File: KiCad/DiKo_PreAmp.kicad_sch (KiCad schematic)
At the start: 17 parts, among them J1 VCC_IN, J2 VCC_OUT, SW1 SW_DPST, U1 REC10K

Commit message: KiCad
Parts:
- added C11: 100nF, symbol Device:C_Small
- added C12, C13: 470pF, symbol Device:C_Small
- added C14, C15: 1nF, symbol Device:C_Small
- added L3: L_Ferrite, symbol Device:L_Ferrite
- added L5: ~, symbol Device:L_Ferrite
- added U2: REC10K-2409, REC10K-2409SAW_H2:CONV_REC10K-2409SAW_H2, symbol REC10K-2409SAW_H2:REC10K-2409SAW_H2
- U1: value REC10K -> REC10K-2415
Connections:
- net FILT_GND: now also C14.1, C15.2
- net GND: now also C11.2, C13.2, C15.1, L5.2
- net at C2.1, C8.2, C9.1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: now also C12.1, U2.1 (+VIN)
- net at C10.1, C2.2, C7.1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: now also C13.1, U2.2 (-VIN)
- new net: L5.1, U2.4 (-VOUT)
- new net: L3.1, U2.6 (+VOUT)
- new net +9V: C11.1, C12.2, C14.2, L3.2
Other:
- moved on the sheet: C10, C3, C4, C5, C6, C9, L1, L2, U1

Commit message: Einpflegen der Eingangsstufe
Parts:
- added C16: 47u, symbol Device:C_Small
- added C17, C18: 0.1uF, symbol Device:C_Small
- added J3: Mic_In, symbol Connector:Conn_01x03_Pin
- added R1, R2: 47k, symbol Device:R_US
- added R3: 100k, symbol Device:R_US
- added R4: 22R, symbol Device:R_US
- added RV1: 10k lin, symbol Device:R_Potentiometer_US
- added U3: INA128U, D0008A_N, symbol INA128U:INA128U
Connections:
- net +15V: now also C18.2, U3.7 (V+)
- net -15V: now also C17.2, U3.4 (V-)
- net GND: now also C17.1, C18.1, J3.1 (Pin_1), R1.2, R2.2, R3.2, U3.5 (REF)
- new net: J3.3 (Pin_3), R1.1, U3.2 (IN-)
- new net: J3.2 (Pin_2), R2.1, U3.3 (IN+)
- new net: C16.1, R3.1
- new net: RV1.1, U3.1 (RG)
- new net: RV1.2, RV1.3, U3.8 (RG)
- new net: C16.2, R4.2
- new net: R4.1, U3.6 (OUT)
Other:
- moved on the sheet: C1, C10, C11, C12, C13, C14, C15, C2, C3, C4, C5, C6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

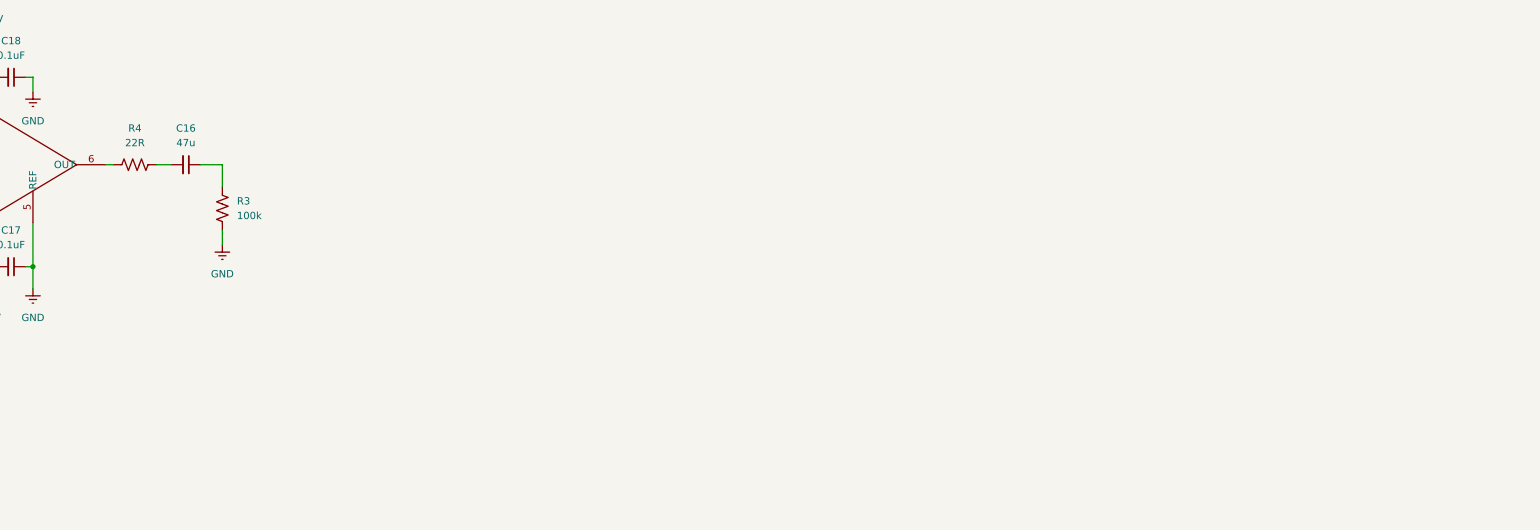
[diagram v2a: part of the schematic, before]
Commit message: Eingangsstufe update
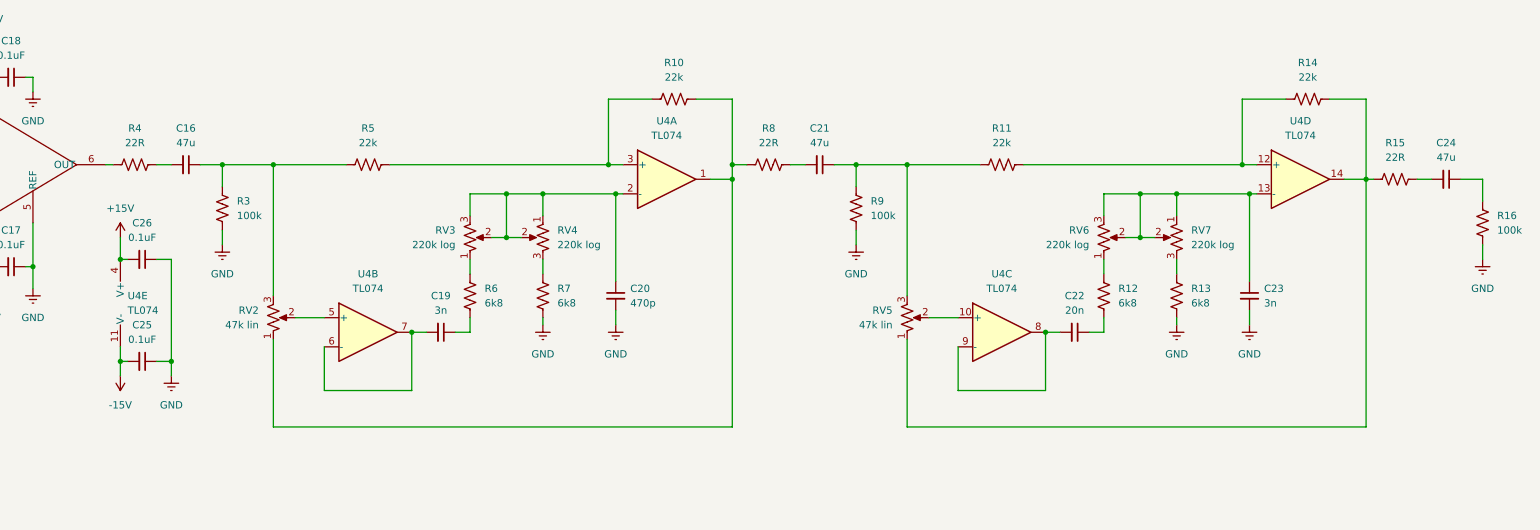
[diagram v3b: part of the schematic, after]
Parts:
- added C19, C23: 3n, symbol Device:C_Small
- added C20: 470p, symbol Device:C_Small
- added C21, C24: 47u, symbol Device:C_Small
- added C22: 20n, symbol Device:C_Small
- added C25, C26: 0.1uF, symbol Device:C_Small
- added R10, R11, R14, R5: 22k, symbol Device:R_US
- added R12, R13, R6, R7: 6k8, symbol Device:R_US
- added R15, R8: 22R, symbol Device:R_US
- added R16, R9: 100k, symbol Device:R_US
- added RV2, RV5: 47k lin, symbol Device:R_Potentiometer_US
- added RV3, RV4, RV6, RV7: 220k log, symbol Device:R_Potentiometer_US
- added U4: TL074, symbol Amplifier_Operational:TL074
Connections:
- net +15V: now also C26.2, U4.4 (V+)
- net -15V: now also C25.2, U4.11 (V-)
- net GND: now also C20.2, C23.2, C25.1, C26.1, R13.2, R16.2, R7.2, R9.2
- net at C16.1, R3.1: now also R5.1, RV2.3
- new net: RV5.2, U4.10 (+)
- new net: C22.2, U4.8, U4.9 (-)
- new net: R6.1, RV3.1
- new net: C20.1, RV3.2, RV3.3, RV4.1, RV4.2, U4.2 (-)
- new net: R10.2, R8.1, RV2.1, U4.1
- new net: RV2.2, U4.5 (+)
- new net: R10.1, R5.2, U4.3 (+)
- new net: C19.2, U4.6 (-), U4.7
- new net: R13.1, RV7.3
- new net: R11.2, R14.1, U4.12 (+)
- new net: C23.1, RV6.2, RV6.3, RV7.1, RV7.2, U4.13 (-)
- new net: R14.2, R15.1, RV5.1, U4.14
- new net: R12.1, RV6.1
- new net: C19.1, R6.2
- new net: C21.1, R11.1, R9.1, RV5.3
- new net: R7.1, RV4.3
- new net: C21.2, R8.2
- new net: C22.1, R12.2
- new net: C24.1, R16.1
- new net: C24.2, R15.2

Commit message: Eingangsstufe Update
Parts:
- added C27, C28, C29, C30, C31, C36, C37, C38, C41, C48, C50, C51, C52, C55, C56, C57: 47u, symbol Device:C_Small
- added C32, C33, C39, C40, C45, C46, C53, C54: 0.1uF, symbol Device:C_Small
- added C34, C35: 330p, symbol Device:C_Small
- added C42: 33u, symbol Device:C_Small
- added C43: 150n, symbol Device:C_Small
- added C44: 470n, symbol Device:C_Small
- added C47, C49: 15p, symbol Device:C_Small
- added J4: R_Line_In, symbol Connector:Conn_01x02_Pin
- added J5: L_Line_In, symbol Connector:Conn_01x02_Pin
- added J6: R_Phono_In, symbol Connector:Conn_01x02_Pin
- added J7: L_Phono_In, symbol Connector:Conn_01x02_Pin
- added J8: Effekt_In, symbol Connector:Conn_01x02_Pin
- added R17: 100R, symbol Device:R_US
- added R18, R21, R22, R24, R27, R33, R34, R38, R42, R47, R49, R51, R54, R61, R64, R71: 100k, symbol Device:R_US
- added R19, R20, R23, R25, R26, R28, R39, R43, R48, R50, R62, R65, R72: 22R, symbol Device:R_US
- added R29, R31: 47k, symbol Device:R_US
- added R30, R32: 0R, symbol Device:R_US
- added R35, R36, R37, R52, R53, R55, R56, R59, R60, R63, R66, R67, R70: 10k, symbol Device:R_US
- added R40, R45: 22k, symbol Device:R_US
- added R41: 1k, symbol Device:R_US
- added R44: 690R, symbol Device:R_US
- added R46: 1k2, symbol Device:R_US
- added R57, R58, R68, R69: 5k, symbol Device:R_US
- added SW2, SW3, SW4: SW_SPDT, symbol Switch:SW_SPDT
- added U5, U6, U7, U8: TL074, symbol Amplifier_Operational:TL074
- R15: value 22R -> 10k
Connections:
- net +15V: now also C32.2, C39.2, C45.2, C53.2, U5.4 (V+), U6.4 (V+), U7.4 (V+), U8.4 (V+)
- net -15V: now also C33.2, C40.2, C46.2, C54.2, U5.11 (V-), U6.11 (V-), U7.11 (V-), U8.11 (V-)
- net GND: now also C32.1, C33.1, C34.2, C35.2, C39.1, C40.1, C42.2, C43.2, C45.1, C46.1, C53.1, C54.1, J4.2 (Pin_2), J5.2 (Pin_2), J6.2 (Pin_2), J7.2 (Pin_2), J8.2 (Pin_2), R18.2, R21.2, R22.2, R24.2, R27.2, R29.2, R31.2, R33.2, R34.2, R38.2, R42.2, R44.2, R46.2, R47.2, R49.2, R51.2, R54.2, R58.1, R61.2, R64.2, R69.1, R71.2, U5.10 (+), U6.10 (+), U7.10 (+), U8.12 (+)
- net at R10.2, RV2.1, U4.1: now also C21.2; no longer R8.1
- net at R5.1, RV2.3: now also R4.2; no longer C16.1, R3.1
- net at R14.2, RV5.1, U4.14: now also C24.2; no longer R15.1
- net at RV1.2, RV1.3: now also R17.1; no longer U3.8 (RG)
- net at R11.1, RV5.3: now also R8.2; no longer C21.1, R9.1
- net at C24.1, R16.1: now also R15.1
- net at R15.2: now also R52.2, R53.1, U7.9 (-); no longer C24.2
- net at C16.2: now also U3.6 (OUT); no longer R4.2
- net at R4.1: now also C16.1, R3.1; no longer U3.6 (OUT)
- new net: C28.1, R20.1, R21.1
- new net: C28.2, U5.1, U5.2 (-)
- new net: C55.1, R61.1, R62.1
- new net: C34.1, J6.1 (Pin_1), R30.1
- new net: C38.1, R38.1, R39.1
- new net: R57.1, R60.1, SW3.2 (B), U7.13 (-)
- new net: R56.1, R60.2, SW3.1 (A), U7.14
- new net: R66.1, R68.1, SW4.2 (B), U5.13 (-)
- new net: R68.2, R69.2, U8.9 (-)
- new net: C30.1, R24.1, R25.1
- new net: C30.2, U5.6 (-), U5.7
- new net: C41.1, R42.1, R43.1
- new net: C41.2, C47.1, R40.1, U6.14
- new net: C29.1, R22.1, R23.1
- new net: R23.2, U5.5 (+)
- new net: R31.1, R32.2, U6.5 (+)
- new net: C37.2, U6.6 (-), U6.7
- new net: R66.2, R67.1, SW4.1 (A), U5.14
- new net: C43.1, C44.1, R43.2, U7.3 (+)
- new net: R50.2, U7.5 (+)
- new net: C51.2, U7.6 (-), U7.7
- new net: R55.2, U7.12 (+)
- new net: C49.1, C50.2, R45.1, U7.1
- new net: C49.2, R45.2, R46.1, U7.2 (-)
- new net: R63.2, U8.5 (+)
- new net: C56.2, U8.6 (-), U8.7
- new net: C56.1, R64.1, R65.1
- new net: R19.2, U5.3 (+)
- new net: C48.1, R49.1, R50.1
- new net: C52.1, R54.1, R55.1, R63.1
- new net: C29.2, J5.1 (Pin_1)
- new net: C57.1, R71.1, R72.1
- new net: C52.2, R53.2, U7.8
- new net: C27.1, R18.1, R19.1
- new net: C27.2, J4.1 (Pin_1)
- new net: R35.2, R36.2, R37.1, U6.9 (-)
- new net: C38.2, R37.2, U6.8
- new net: C31.2, R26.2, U5.8
- new net: R20.2, R25.2, R26.1, U5.9 (-)
- new net: C37.1, R34.1, R36.1
- new net: R67.2, R70.1, U8.10 (+)
- new net: C57.2, R70.2, U8.8
- new net: R56.2, R59.1, U8.2 (-)
- new net: C55.2, R59.2, U8.1
- new net: C48.2, J8.1 (Pin_1)
- new net: C51.1, R51.1, R52.1
- new net: R48.2, SW2.1 (A)
- new net: SW2.2 (B), U5.12 (+)
- new net: R28.2, SW2.3 (C)
- new net: C44.2, R44.1
- new net: C21.1, R8.1, R9.1
- new net: C47.2, R40.2, R41.1, U6.13 (-)
- new net: C31.1, R27.1, R28.1
- new net: R57.2, R58.2, U8.3 (+)
- new net: C36.1, R33.1, R35.1
- new net: C42.1, R41.2
- new net: C35.1, J7.1 (Pin_1), R32.1
- new net: R39.2, U6.12 (+)
- new net: R17.2, U3.8 (RG)
- new net: C50.1, R47.1, R48.1
- new net: C36.2, U6.1, U6.2 (-)
- new net: R29.1, R30.2, U6.3 (+)
- new net: U8.13 (-), U8.14
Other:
- moved on the sheet: C16, C17, C18, C19, C20, C21, C22, C23, C24, C25, C26, J3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

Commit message: Schaltplan Update
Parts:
- removed C21, C24, C27, C28, C29, C30, C37, C38, C41, C52, C55, C56, C57: 47u, symbol Device:C_Small
- removed C42: 33u, symbol Device:C_Small
- removed C44: 470n, symbol Device:C_Small
- removed R1: 47k, symbol Device:R_US
- removed R18, R21, R24, R38, R49, R71: 100k, symbol Device:R_US
- removed R23, R39, R43, R48, R65, R72, R8: 22R, symbol Device:R_US
- removed R63: 10k, symbol Device:R_US
- added C1, C14, C7: 2n2, symbol Device:C_Small
- added C12: 30n, symbol Device:C_Small
- added C13: 91n, symbol Device:C_Small
- added C32, C33, C46, C47: 100n, symbol Device:C_Small
- added C4: 130n, symbol Device:C_Small
- added C5: 390n, symbol Device:C_Small
- added C6: 750p, symbol Device:C_Small
- added J7: AUX_RET_1, symbol Connector:Conn_01x02_Pin
- added J8: AUX_RET_2, symbol Connector:Conn_01x02_Pin
- added J9: AUX_RET_3, symbol Connector:Conn_01x02_Pin
- added R10, R37, R40, R60, R67, R7, R77, R78, R79, R80: 10k, symbol Device:R_US
- added R11: 560R, symbol Device:R_US
- added R12, R26, R41, R56: 22k, symbol Device:R_US
- added R13, R57: 470, symbol Device:R_US
- added R14, R59: 1k, symbol Device:R_US
- added R53, R6: 4k7, symbol Device:R_US
- added R68, R69: 6k8, symbol Device:R_US
- added RV1, RV10, RV18, RV5, RV6: 50k log, symbol Device:R_Potentiometer_US
- added RV14, RV15: 47k log, symbol Device:R_Potentiometer_US
- added RV17, RV23, RV4, RV9: 47k lin, symbol Device:R_Potentiometer_US
- added RV19, RV20: 470k log, symbol Device:R_Potentiometer_US
- added RV2, RV3, RV7, RV8: 22k log, symbol Device:R_Potentiometer_US
- added SW1, SW3, SW5: SW_SPDT, symbol Switch:SW_SPDT
- added U11, U12, U4, U5, U7, U8: TL074, symbol Amplifier_Operational:TL074
- added Z1, Z10, Z100, Z101, Z102, Z103, Z104, Z105, Z106, Z107, Z108, Z109, Z11, Z110, Z111, Z112, Z113, Z114, Z115, Z116, Z117, Z118, Z119, Z12, Z13, Z14, Z15, Z16, Z17, Z18, Z19, Z2, Z20, Z21, Z22, Z23, Z24, Z25, Z26, Z27, Z28, Z29, Z3, Z30, Z31, Z32, Z33, Z34, Z35, Z36, Z37, Z38, Z39, Z4, Z40, Z41, Z42, Z43, Z44, Z45, Z46, Z47, Z48, Z49, Z5, Z50, Z51, Z52, Z53, Z54, Z55, Z56, Z57, Z58, Z59, Z6, Z60, Z61, Z62, Z63, Z64, Z65, Z66, Z67, Z68, Z69, Z7, Z70, Z71, Z72, Z73, Z74, Z75, Z76, Z77, Z78, Z79, Z8, Z80, Z81, Z82, Z83, Z84, Z85, Z86, Z87, Z88, Z89, Z9, Z90, Z91, Z92, Z93, Z94, Z95, Z96, Z97, Z98, Z99: ~, symbol Device:R_Small
- C16: value 47u -> 6n8
- C18: renamed from C12; value 470pF -> 470p
- C19: renamed from C14; value 1nF -> 1n
- C20: renamed from C11; value 100nF -> 100n
- C21: renamed from C15; value 1nF -> 1n
- C22: renamed from C13; value 470pF -> 470p
- C23: renamed from C9; value 470pF -> 470p
- C24: renamed from C8; value 10nF -> 10n
- C25: renamed from C3; value 1nF -> 1n
- C26: renamed from C39; value 0.1uF -> 100n
- C27: renamed from C45; value 0.1uF -> 100n
- C28: renamed from C32; value 0.1uF -> 100n
- C29: renamed from C26; value 0.1uF -> 100n
- C3: renamed from C47; value 15p -> 47n
- C30: renamed from C53; value 0.1uF -> 100n
- C31, C36, C48, C50, C51: value 47u -> 100n
- C34, C35: value 330p -> 100n
- C37: renamed from C4; value 100nF -> 100n
- C38: renamed from C1; value 10uF -> 10u
- C39: renamed from C2; value 10uF -> 10u
- C40: renamed from C5; value 100nF -> 100n
- C41: renamed from C40; value 0.1uF -> 100n
- C42: renamed from C46; value 0.1uF -> 100n
- C43: renamed from C33; value 0.1uF -> 100n
- C44: renamed from C25; value 0.1uF -> 100n
- C45: renamed from C54; value 0.1uF -> 100n
- C49: value 15p -> 100n
- C52: renamed from C7; value 10nF -> 10n
- C53: renamed from C6; value 1nF -> 1n
- C54: renamed from C10; value 470pF -> 470p
- R15, R35, R52: value 10k -> 6k8
- R16, R34, R51: value 100k -> 6k8
- R17: renamed from R67; value 10k -> 4k7
- R19, R4: value 22R -> 4k7
- R2: value 47k -> 33k
- R20, R25, R28, R50: value 22R -> 10k
- R21: renamed from R68; value 5k -> 470
- R22, R3, R33, R54, R61, R64: value 100k -> 10k
- R23: renamed from R26; value 22R -> 10k
- R24: renamed from R69; value 5k -> 1k
- R27, R42: value 100k -> 470
- R29: value 47k -> 1k
- R30: value 0R -> 10k
- R31: value 47k -> 10k
- R32: value 0R -> 22k
- R36: value 10k -> 4k7
- R44: value 690R -> 1k
- R45: value 22k -> 10k
- R46: value 1k2 -> 10k
- R47, R9: value 100k -> 22k
- R5: renamed from R40; value 22k -> 68k
- R62: value 22R -> 22k
- R8: renamed from R41; value 1k -> 6k8
- renumbered C20 to C10, C19 to C11, C23 to C15, C22 to C17, C43 to C2, C18 to C8, C17 to C9, J6 to J1, J1 to J10, J2 to J11, J7 to J2, J4 to J3, J5 to J4, J3 to J5, J8 to J6, L3 to L1, L5 to L2, L1 to L3, L2 to L5, R37 to R1, R70 to R18, R10 to R38, R5 to R39, R17 to R43, R6 to R48, R7 to R49, R14 to R58, R11 to R63, R53 to R65, R12 to R70, R13 to R71, R56 to R72, R59 to R73, R60 to R74, R57 to R75, R58 to R76, RV1 to RV11, RV3 to RV12, RV4 to RV13, RV2 to RV16, RV6 to RV21, RV7 to RV22, RV5 to RV24, SW3 to SW6, SW1 to SW7, U6 to U1, U4 to U10, U2 to U13, U1 to U14, U7 to U2, U8 to U3, U5 to U6, U3 to U9
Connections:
- net +15V: now also C31.2, C34.2, C35.2, C36.2, C32.2, C33.2, U11.4 (V+), U12.4 (V+), U4.4 (V+), U5.4 (V+), U7.4 (V+), U8.4 (V+)
- net -15V: now also C48.2, C49.2, C50.2, C51.2, C46.2, C47.2, U11.11 (V-), U12.11 (V-), U4.11 (V-), U5.11 (V-), U7.11 (V-), U8.11 (V-)
- net GND: now also C31.1, C34.1, C35.1, C36.1, C48.1, C49.1, C50.1, C51.1, R29.1, R35.2, R44.1, R52.2, C12.2, C14.2, C32.1, C33.1, C4.2, C46.1, C47.1, C6.2, J7.2 (Pin_2), J8.2 (Pin_2), J9.2 (Pin_2), R11.2, R14.1, R59.1, R69.2, Z103.1, Z104.1, Z105.1, Z106.1, Z107.1, Z11.1, Z111.1, Z112.1, Z113.1, Z117.1, Z118.1, Z119.1, Z12.1, Z13.1, Z14.1, Z18.1, Z19.1, Z20.1, Z23.1, Z26.1, Z29.1, Z35.1, Z36.1, Z37.1, Z38.1, Z4.1, Z41.1, Z44.1, Z45.1, Z49.1, Z5.1, Z50.1, Z51.1, Z52.1, Z54.1, Z55.1, Z62.1, Z63.1, Z64.1, Z68.1, Z69.1, Z70.1, Z71.1, Z74.1, Z77.1, Z8.1, Z84.1, Z85.1, Z86.1, Z87.1, Z88.1, Z91.1, Z95.1, Z96.1, Z97.1; no longer C2.2, C34.2, C35.2, R2.2, R22.2, R27.2, R29.2, R3.2, R31.2, R33.2, R34.2, R42.2, R44.2, R46.2, R47.2, R51.2, R54.2, R61.2, R64.2, R9.2, U1.10 (+), U2.10 (+), U3.12 (+), U6.10 (+)
- net at R20.1: now also R19.2, U4.9 (-)
- net at U6.1, U6.2 (-): now also Z31.2
- net at R61.1: now also R55.2, R66.2, R60.2, U5.6 (-); no longer R62.1
- net at J5.3 (Pin_3): now also Z53.2, Z54.2; no longer U9.2 (IN-)
- net at R21.1, U6.13 (-): now also RV5.2, RV5.3; no longer R66.1, SW4.2 (B)
- net at R25.1: now also Z40.1
- net at U6.6 (-), U6.7: now also Z47.2
- net at R42.1: now also SW4.2 (B), RV10.2, RV10.3, U4.13 (-)
- net at C3.1, R5.1, U1.14: now also Z9.2
- net at R22.1: now also Z32.1
- net at U6.5 (+): now also Z46.1, Z50.2
- net at U1.6 (-), U1.7: now also Z16.2
- net at R17.1, U6.14: now also RV5.1; no longer R66.2, SW4.1 (A)
- net at C2.1: now also R4.2; no longer U2.3 (+)
- net at R50.2: now also R45.2, R46.1, R40.2, U5.2 (-); no longer U2.5 (+)
- net at U2.6 (-), U2.7: now also Z93.2; no longer C51.2
- net at U2.12 (+): now also U3.5 (+), Z81.1; no longer R55.2
- net at U3.6 (-), U3.7: now also Z82.2
- net at C10.1, RV12.2, RV12.3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: now also U10.3 (+); no longer U10.2 (-)
- net at R38.2, RV16.1, U10.1: now also Z60.2
- net at R39.1, RV16.3: now also Z57.1; no longer R4.2
- net at R64.1: now also Z79.1
- net at U6.3 (+): now also Z30.1, Z36.2; no longer R19.2
- net at R50.1: now also R33.1, R66.1, Z102.1; no longer C48.1
- net at R54.1: now also R53.2, U8.9 (-); no longer R55.1
- net at R38.1, R39.2: now also U10.2 (-); no longer U10.3 (+)
- net at J4.1 (Pin_1): now also Z46.2, Z49.2
- net at R65.1, U2.9 (-): now also R64.2, R67.2; no longer R15.2, R52.2
- net at R65.2, U2.8: now also Z80.2
- net at R19.1: now also RV6.1, SW3.1 (A), U4.7
- net at J3.1 (Pin_1): now also Z30.2, Z35.2
- net at R58.1, R63.2: now also U10.13 (-); no longer U10.12 (+)
- net at C15.1, RV21.2, RV21.3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: now also U10.12 (+); no longer U10.13 (-)
- net at R58.2, RV24.1, U10.14: now also Z78.2
- net at R1.1, U1.9 (-): now also R3.2, R10.2; no longer R35.2, R36.2
- net at R1.2, U1.8: now also Z6.2
- net at R23.2, U6.8: now also Z33.2; no longer C31.2
- net at R23.1, U6.9 (-): now also R22.2, R28.2; no longer R20.2, R25.2
- net at R62.2: now also R56.1, U11.2 (-)
- net at R34.1: now also RV7.1; no longer R36.1
- net at R18.2, U3.8: now also Z27.2
- net at R73.2, U3.1: now also Z89.2
- net at J6.1 (Pin_1): now also Z92.2, Z95.2; no longer C48.2
- net at SW2.1 (A): now also Z25.1
- net at SW2.3 (C): now also Z34.1; no longer R28.2
- net at R63.1, RV24.3: now also Z61.1
- net at R9.1: now also R12.2, U5.9 (-)
- net at C3.2, R5.2, R8.1: no longer U1.13 (-)
- net at R8.2: now also U1.13 (-), R11.1
- net at U1.12 (+): now also Z7.1
- net at R15.1: now also RV2.1; no longer R16.1
- net at R47.1: now also RV17.3, Z67.1; no longer C50.1
- net at U1.1, U1.2 (-): now also Z2.2; no longer C36.2
- net at C16.2: now also U11.6 (-), U11.7; no longer U9.6 (OUT)
- net at U3.14: now also R6.1, RV1.1, SW1.1 (A); no longer U3.13 (-)
- new net: R46.2, U5.1, Z66.2
- new net: J7.1 (Pin_1), Z103.2, Z98.2
- new net: Z31.1, Z32.2, Z37.2
- new net: R67.1, Z94.1
- new net: C5.1, R15.2
- new net: J1.1 (Pin_1), Z1.2, Z4.2
- new net: R40.1, Z59.1
- new net: Z58.1, Z59.2, Z63.2
- new net: Z47.1, Z48.2, Z51.2
- new net: C4.1, RV2.2, RV2.3, RV3.1, RV3.2, U5.10 (+)
- new net: R7.2, U4.1, Z21.2
- new net: R6.2, R7.1, U4.2 (-)
- new net: R13.2, R14.2, U4.3 (+)
- new net: U3.12 (+), U4.12 (+), U4.5 (+), U8.5 (+), Z28.1
- new net: Z27.1, Z28.2, Z29.2
- new net: R53.1, RV18.1, SW5.1 (A), U8.7
- new net: R57.1, RV18.2, RV18.3, SW5.2 (B), U8.6 (-)
- new net: Z101.1, Z102.2, Z106.2
- new net: R78.2, U12.7, Z101.2
- new net: C7.1, R34.2
- new net: R68.1, RV19.1
- new net: C14.1, RV19.2, RV19.3, RV20.1, RV20.2, U11.3 (+)
- new net: U1.5 (+), Z15.1, Z19.2
- new net: U2.5 (+), Z92.1, Z96.2
- new net: R77.2, R78.1, R79.2, R80.2, U12.6 (-)
- new net: C1.1, C2.2, R2.1, U2.2 (-)
- new net: R4.1, Z10.1
- new net: Z10.2, Z12.2, Z9.1
- new net: R25.2, R30.2, R31.1, R33.2, U8.13 (-)
- new net: C1.2, R2.2, U2.1, Z24.2
- new net: U2.3 (+), Z14.2
- new net: J2.1 (Pin_1), Z15.2, Z18.2
- new net: R37.2, U8.1, Z58.2
- new net: J8.1 (Pin_1), Z108.2, Z111.2
- new net: R54.2, U8.8, Z72.2
- new net: Z78.1, Z79.2, Z84.2
- new net: Z60.1, Z61.2, Z64.2
- new net: Z39.1, Z40.2, Z41.2
- new net: J5.2 (Pin_2), Z65.2, Z68.2
- new net: Z66.1, Z67.2, Z70.2
- new net: R9.2, RV4.1, U5.8
- new net: R28.1, Z48.1
- new net: R79.1, Z110.1
- new net: Z2.1, Z3.2, Z8.2
- new net: U11.12 (+), Z108.1, Z112.2
- new net: U1.3 (+), Z1.1, Z5.2
- new net: Z89.1, Z90.2, Z91.2
- new net: R26.2, RV9.1, U7.1
- new net: R26.1, R32.2, U7.2 (-)
- new net: C6.1, RV7.2, RV7.3, RV8.1, RV8.2, U7.3 (+)
- new net: R16.1, RV3.3
- new net: R42.2, R44.2, U8.3 (+)
- new net: U1.10 (+), Z13.2
- new net: U5.5 (+), Z87.2
- new net: R61.2, U5.7, Z75.2
- new net: U6.10 (+), Z45.2
- new net: U11.10 (+), Z104.2, Z98.1
- new net: R3.1, Z3.1
- new net: Z72.1, Z73.2, Z74.2
- new net: R62.1, RV23.3, Z76.1
- new net: C16.1, R68.2
- new net: U9.3 (IN+), Z65.1, Z69.2
- new net: R51.1, RV14.1
- new net: C12.1, RV14.2, RV14.3, RV15.1, RV15.2, U7.10 (+)
- new net: R52.1, RV15.3
- new net: Z115.1, Z116.2, Z119.2
- new net: U12.1, U12.2 (-), Z115.2
- new net: Z80.1, Z81.2, Z85.2
- new net: R80.1, Z116.1
- new net: Z82.1, Z83.2, Z86.2
- new net: Z100.2, Z105.2, Z99.1
- new net: U11.8, U11.9 (-), Z99.2
- new net: R36.1, RV10.1, SW4.1 (A), U4.14
- new net: R41.2, RV17.1, U7.8
- new net: R41.1, R47.2, U7.9 (-)
- new net: R20.2, U4.8, Z39.2
- new net: R27.2, R29.2, U4.10 (+)
- new net: C13.1, R51.2
- new net: C13.2, U7.13 (-), U7.14
- new net: R27.1, RV6.2, RV6.3, SW3.2 (B), U4.6 (-)
- new net: Z11.2, Z6.1, Z7.2
- new net: R36.2, R37.1, U8.2 (-)
- new net: U2.10 (+), Z88.2
- new net: Z24.1, Z25.2, Z26.2
- new net: R57.2, R59.2, U8.10 (+)
- new net: Z42.1, Z43.2, Z44.2
- new net: R31.2, U8.14, Z42.2
- new net: Z75.1, Z76.2, Z77.2
- new net: Z16.1, Z17.2, Z20.2
- new net: R13.1, RV1.2, RV1.3, SW1.2 (B), U3.13 (-)
- new net: U11.13 (-), U11.14, Z109.2
- new net: R77.1, Z100.1
- new net: RV9.2, U7.5 (+)
- new net: R32.1, RV9.3, Z43.1
- new net: Z21.1, Z22.2, Z23.2
- new net: U8.12 (+), Z52.2
- new net: Z109.1, Z110.2, Z113.2
- new net: RV23.2, U11.5 (+)
- new net: RV17.2, U7.12 (+)
- new net: U9.2 (IN-), Z53.1, Z55.2
- new net: R69.1, RV20.3
- new net: Z56.1, Z57.2, Z62.2
- new net: U12.5 (+), Z107.2
- new net: J9.1 (Pin_1), Z114.2, Z117.2
- new net: R56.2, RV23.1, U11.1
- new net: C7.2, U7.6 (-), U7.7
- new net: Z33.1, Z34.2, Z38.2
- new net: Z93.1, Z94.2, Z97.2
- new net: RV4.2, U5.12 (+)
- new net: C5.2, U5.13 (-), U5.14
- new net: R55.1, Z73.1
- new net: U5.3 (+), Z71.2
- new net: U12.3 (+), Z114.1, Z118.2
- new net: R35.1, RV8.3
- new net: U9.6 (OUT), Z56.2
- new net: R12.1, RV4.3, Z22.1
- new net: R10.1, Z17.1
- new net AUX_MIC_EFFEKT: Z90.1
- new net KST_1_2: R30.1, R45.1, R60.1, Z83.1
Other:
- moved on the sheet: C10, C11, C15, C17, C2, C26, C27, C28, C29, C3, C30, C41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

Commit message: Schaltplan Update
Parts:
- added C12, C13, C14, C15, C16, C17, C18, C19, C22, C23, C25, C26, C27, C28, C32, C33, C36, C37, C38, C39, C4, C40, C41, C42, C43, C47, C48, C5, C6, C7, C8, C9: 130n, symbol Device:C_Small
- added C69, C70, C71, C72, C88, C89, C90, C91: 100n, symbol Device:C_Small
- added R100, R101, R13, R14, R21, R22, R23, R24, R32, R33, R39, R40, R48, R49, R50, R51, R55, R56, R62, R63, R73, R74, R75, R76, R79, R8, R80, R85, R86, R9, R98, R99: 6k8, symbol Device:R_US
- added U12, U13, U16, U17, U19, U20: TL074, symbol Amplifier_Operational:TL074
- added unit 5 of U15
- added unit 4 of U7
- added unit 3 of U7
- added unit 4 of U9
- added unit 3 of U9
- added Z101, Z102, Z104, Z117, Z118, Z119, Z120, Z122, Z123, Z15, Z16, Z20, Z27, Z28, Z29, Z30, Z33, Z34, Z50, Z51, Z53, Z64, Z65, Z66, Z67, Z69, Z70, Z78, Z79, Z84, Z92, Z93, Z94, Z95, Z97, Z98: ~, symbol Device:R_Small
- renumbered C4 to C10, C5 to C11, C6 to C20, C7 to C21, C8 to C24, C9 to C29, C10 to C30, C11 to C31, C12 to C34, C13 to C35, C14 to C44, C15 to C45, C16 to C46, C17 to C49, C18 to C50, C19 to C51, C20 to C52, C21 to C53, C22 to C54, C23 to C55, C24 to C56, C25 to C57, C26 to C58, C27 to C59, C28 to C60, C29 to C61, C30 to C62, C31 to C63, C32 to C64, C33 to C65, C34 to C66, C35 to C67, C36 to C68, C37 to C73, C38 to C74, C39 to C75, C40 to C76, C41 to C77, C42 to C78, C43 to C79, C44 to C80, C45 to C81, C46 to C82, C47 to C83, C48 to C84, C49 to C85, C50 to C86, C51 to C87, C52 to C92, C53 to C93, C54 to C94, R8 to R10, R70 to R102, R71 to R103, R72 to R104, R73 to R105, R74 to R106, R75 to R107, R76 to R108, R77 to R109, R9 to R11, R78 to R110, R79 to R111, R80 to R112, R10 to R12, R11 to R15, R12 to R16, R13 to R17, R14 to R18, R15 to R19, R16 to R20, R17 to R25, R18 to R26, R19 to R27, R20 to R28, R21 to R29, R22 to R30, R23 to R31, R24 to R34, R25 to R35, R26 to R36, R27 to R37, R28 to R38, R29 to R41, R30 to R42, R31 to R43, R32 to R44, R33 to R45, R34 to R46, R35 to R47, R36 to R52, R37 to R53, R38 to R54, R39 to R57, R40 to R58, R41 to R59, R42 to R60, R43 to R61, R44 to R64, R45 to R65, R46 to R66, R47 to R67, R48 to R68, R49 to R69, R50 to R70, R51 to R71, R52 to R72, R53 to R77, R54 to R78, R55 to R81, R56 to R82, R57 to R83, R58 to R84, R59 to R87, R60 to R88, R61 to R89, R62 to R90, R63 to R91, R64 to R92, R65 to R93, R66 to R94, R67 to R95, R68 to R96, R69 to R97, U11 to U10, U7 to U10, U8 to U11, U12 to U11, U9 to U14, U10 to U15, U11 to U18, U13 to U21, U14 to U22, U12 to U4, U4 to U5, U6 to U5, U5 to U6, U8 to U6, U10 to U7, U6 to U8, U5 to U8, U7 to U9, Z73 to Z100, Z74 to Z103, Z75 to Z105, Z76 to Z106, Z77 to Z107, Z78 to Z108, Z79 to Z109, Z80 to Z110, Z81 to Z111, Z82 to Z112, Z83 to Z113, Z84 to Z114, Z85 to Z115, Z86 to Z116, Z87 to Z121, Z88 to Z124, Z89 to Z125, Z90 to Z126, Z91 to Z127, Z92 to Z128, Z93 to Z129, Z94 to Z130, Z95 to Z131, Z96 to Z132, Z97 to Z133, Z98 to Z134, Z99 to Z135, Z100 to Z136, Z101 to Z137, Z102 to Z138, Z103 to Z139, Z104 to Z140, Z105 to Z141, Z106 to Z142, Z107 to Z143, Z108 to Z144, Z109 to Z145, Z110 to Z146, Z111 to Z147, Z112 to Z148, Z113 to Z149, Z114 to Z150, Z115 to Z151, Z116 to Z152, Z117 to Z153, Z118 to Z154, Z119 to Z155, Z15 to Z17, Z16 to Z18, Z17 to Z19, Z18 to Z21, Z19 to Z22, Z20 to Z23, Z21 to Z24, Z22 to Z25, Z23 to Z26, Z24 to Z31, Z25 to Z32, Z26 to Z35, Z27 to Z36, Z28 to Z37, Z29 to Z38, Z30 to Z39, Z31 to Z40, Z32 to Z41, Z33 to Z42, Z34 to Z43, Z35 to Z44, Z36 to Z45, Z37 to Z46, Z38 to Z47, Z39 to Z48, Z40 to Z49, Z41 to Z52, Z42 to Z54, Z43 to Z55, Z44 to Z56, Z45 to Z57, Z46 to Z58, Z47 to Z59, Z48 to Z60, Z49 to Z61, Z50 to Z62, Z51 to Z63, Z52 to Z68, Z53 to Z71, Z54 to Z72, Z55 to Z73, Z56 to Z74, Z57 to Z75, Z58 to Z76, Z59 to Z77, Z60 to Z80, Z61 to Z81, Z62 to Z82, Z63 to Z83, Z64 to Z85, Z65 to Z86, Z66 to Z87, Z67 to Z88, Z68 to Z89, Z69 to Z90, Z70 to Z91, Z71 to Z96, Z72 to Z99
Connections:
- net +15V: now also C69.2, C70.2, C71.2, C72.2, U12.4 (V+), U13.4 (V+), U15.4 (V+), U16.4 (V+)
- net -15V: now also C88.2, C89.2, C90.2, C91.2, U12.11 (V-), U13.11 (V-), U15.11 (V-), U16.11 (V-)
- net GND: now also C12.1, C13.1, C22.1, C23.1, C36.1, C37.1, C47.1, C48.1, C69.1, C70.1, C71.1, C72.1, C88.1, C89.1, C90.1, C91.1, R13.2, R14.2, R39.2, R40.2, R62.2, R63.2, R85.2, R86.2, Z104.1, Z122.1, Z123.1, Z20.1, Z33.1, Z34.1, Z53.1, Z69.1, Z70.1, Z84.1, Z97.1, Z98.1
- net at R11.2, RV4.1, U6.8: now also Z15.2
- net at R36.2, RV9.1, U10.1: now also Z50.2
- net at R59.2, RV17.1, U10.8: now also Z78.2
- net at R82.2, RV23.1, U18.1: now also Z101.2
- net at U4.12 (+): now also C7.2, R14.1
- net at U4.13 (-): now also U4.14, R9.1, Z27.2
- net at U4.10 (+): now also C5.2, R13.1
- net at U4.8: now also U4.9 (-), C6.1, R8.1
- new net: R48.1, Z65.1
- new net: C18.1, R48.2, R49.1
- new net: C28.2, R63.1, U13.12 (+)
- new net: R56.1, U13.13 (-), U13.14, Z92.2
- new net: R98.1, Z118.1
- new net: C42.1, R98.2, R99.1
- new net: Z101.1, Z102.2, Z104.2
- new net: C14.2, C15.1, R32.2
- new net: C15.2, R39.1, U9.10 (+)
- new net: Z119.1, Z120.2, Z123.2
- new net: Z29.1, Z30.2, Z34.2
- new net: C32.2, R75.1, U16.8, U16.9 (-)
- new net: C33.1, R75.2, R76.1
- new net: C32.1, R73.2, R74.1
- new net: C36.2, R74.2, U16.10 (+)
- new net: C25.2, C26.1, R55.2
- new net: C26.2, R62.1, U13.10 (+)
- new net: C13.2, R24.2, U7.12 (+)
- new net: C9.2, U7.13 (-), U7.14, Z29.2
- new net: Z92.1, Z93.2, Z97.2
- new net: R80.1, U17.13 (-), U17.14, Z117.2
- new net: C40.2, C41.1, R80.2
- new net: Z15.1, Z16.2, Z20.2
- new net: C37.2, R76.2, U16.12 (+)
- new net: C27.1, R55.1, U13.8, U13.9 (-)
- new net: C27.2, C28.1, R56.2
- new net: C47.2, R99.2, U19.10 (+)
- new net: C43.2, U19.13 (-), U19.14, Z119.2
- new net: C25.1, Z79.1
- new net: Z117.1, Z118.2, Z122.2
- new net: C8.1, R21.2, R22.1
- new net: C8.2, R23.1, U7.8, U7.9 (-)
- new net: C4.1, Z16.1
- new net: C4.2, C5.1, R8.2
- new net: R21.1, Z28.1
- new net: Z78.1, Z79.2, Z84.2
- new net: Z50.1, Z51.2, Z53.2
- new net: C19.1, R50.2, R51.1
- new net: C23.2, R51.2, U12.12 (+)
- new net: Z27.1, Z28.2, Z33.2
- new net: C18.2, R50.1, U12.8, U12.9 (-)
- new net: C43.1, R100.2, R101.1
- new net: C22.2, R49.2, U12.10 (+)
- new net: C48.2, R101.2, U19.12 (+)
- new net: C6.2, C7.1, R9.2
- new net: Z94.1, Z95.2, Z98.2
- new net: Z64.1, Z65.2, Z69.2
- new net: C17.2, R40.1, U9.12 (+)
- new net: R33.1, U9.13 (-), U9.14, Z64.2
- new net: C12.2, R22.2, U7.10 (+)
- new net: C42.2, R100.1, U19.8, U19.9 (-)
- new net: R73.1, Z93.1
- new net: C16.1, R32.1, U9.8, U9.9 (-)
- new net: C16.2, C17.1, R33.2
- new net: C41.2, R86.1, U17.12 (+)
- new net: C38.1, Z102.1
- new net: C38.2, C39.1, R79.2
- new net: Z66.1, Z67.2, Z70.2
- new net: C9.1, R23.2, R24.1
- new net: C14.1, Z51.1
- new net: C33.2, U16.13 (-), U16.14, Z94.2
- new net: C39.2, R85.1, U17.10 (+)
- new net: C19.2, U12.13 (-), U12.14, Z66.2
- new net: C40.1, R79.1, U17.8, U17.9 (-)
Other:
- moved on the sheet: C50, C51, C52, C53, C54, C55, C56, C57, C58, C59, C60, C61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

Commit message: Schaltplan Update
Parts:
- added C95: 470p, symbol Device:C_Small
- added C96: 3n, symbol Device:C_Small
- added C97, C98: 100n, symbol Device:C_Small
- added R113, R114: 22k, symbol Device:R_US
- added R115, R116: 6k8, symbol Device:R_US
- added R117, R118, R119: 10k, symbol Device:R_US
- added R120, R121: 5k, symbol Device:R_US
- added RV25, RV26: 220k log, symbol Device:R_Potentiometer_US
- added RV27: 47k lin, symbol Device:R_Potentiometer_US
- added SW8: SW_SPDT, symbol Switch:SW_SPDT
- added unit 5 of U18
- added U23: TL074, symbol Amplifier_Operational:TL074
- added unit 1 of U7
- added unit 2 of U7
- added Z156, Z157, Z158, Z159, Z160, Z161: ~, symbol Device:R_Small
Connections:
- net +15V: now also C97.2, U18.4 (V+)
- net -15V: now also C98.2, U18.11 (V-)
- net GND: now also U20.12 (+), U20.13 (-), C95.1, C95.2, C97.1, C98.1, R113.1, R114.2, R116.2, R121.1, RV25.2, RV25.3, RV26.1, RV26.2, Z160.1, Z161.1
- net at U11.5 (+), U3.12 (+), U5.12 (+)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: now also U7.3 (+)
- net at U20.14: now also R113.2, RV27.1, Z158.2
- net at U20.10 (+): now also RV27.2
- net at U20.8: now also U20.9 (-), C96.2
- net KST_1_2: no longer names the net of R42.1, R65.1, R88.1, Z113.1
- new net: Z158.1, Z159.2, Z161.2
- new net: R114.1, RV27.3, Z157.1
- new net: R115.1, RV25.1
- new net: C96.1, R115.2
- new net: R119.1, R120.1, SW8.2 (B), U7.2 (-)
- new net: R117.1, R119.2, SW8.1 (A), U7.1
- new net: R116.1, RV26.3
- new net: R117.2, R118.1, U7.6 (-)
- new net: R120.2, R121.2, U7.5 (+)
- new net: Z156.1, Z157.2, Z160.2
- new net: R118.2, Z156.2
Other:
- moved on the sheet: C1, C10, C11, C12, C13, C14, C15, C16, C17, C18, C19, C2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
